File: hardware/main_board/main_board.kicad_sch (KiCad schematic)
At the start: 4 parts

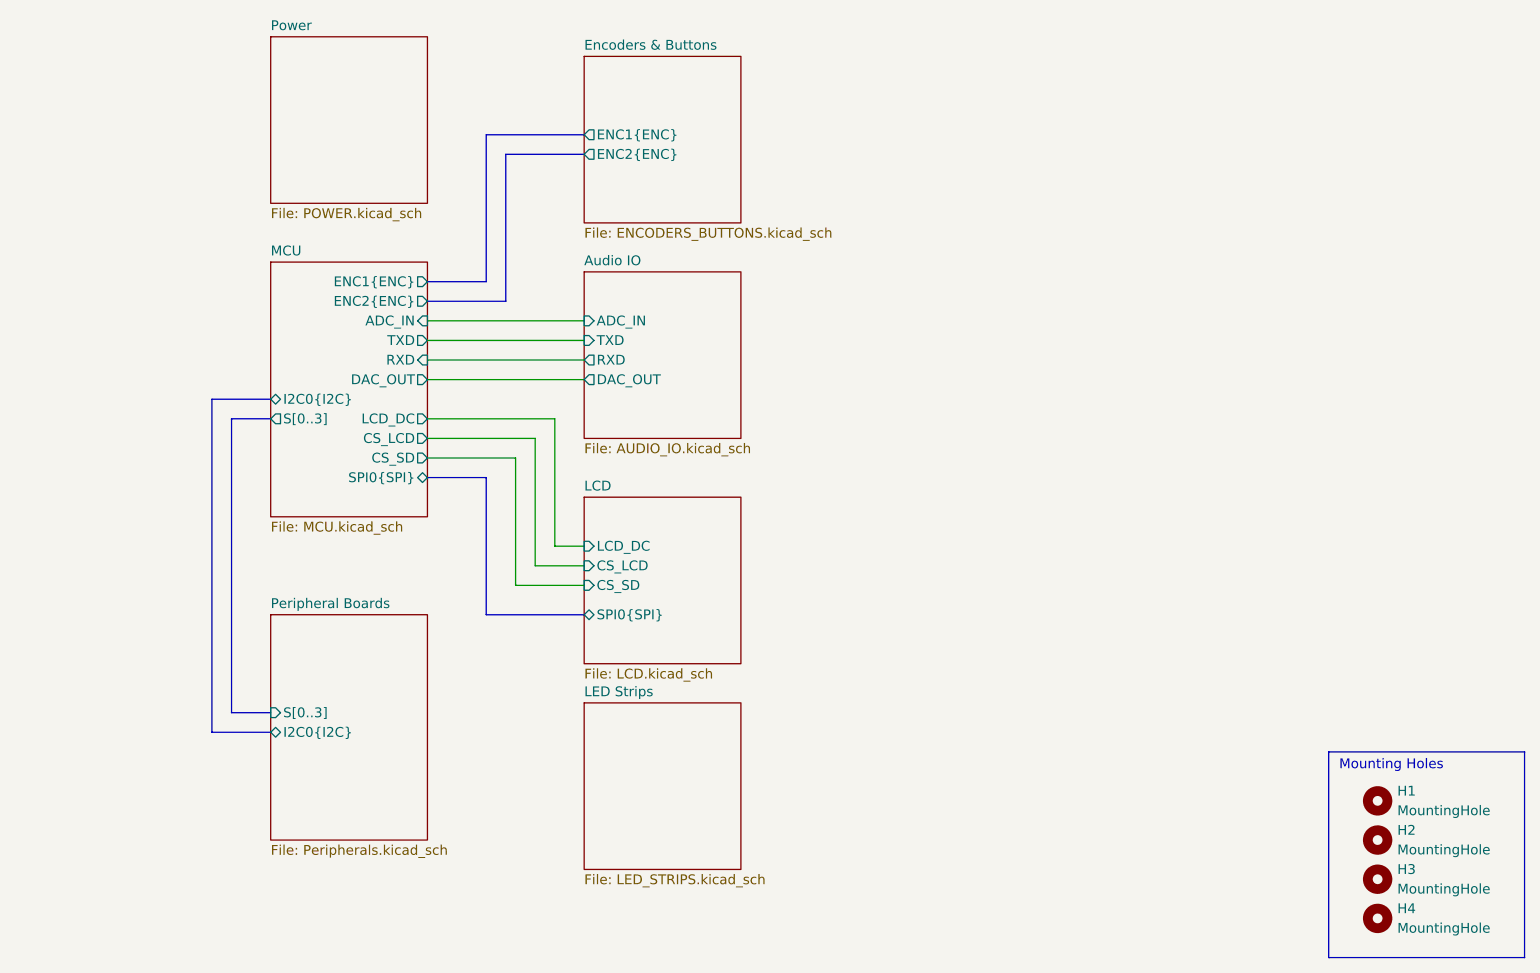
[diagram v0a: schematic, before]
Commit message: added lakshay suggestions to peripheral board. removed bypass jumper from main board audio amp. added led strip interface. added too many things to remember i forgor
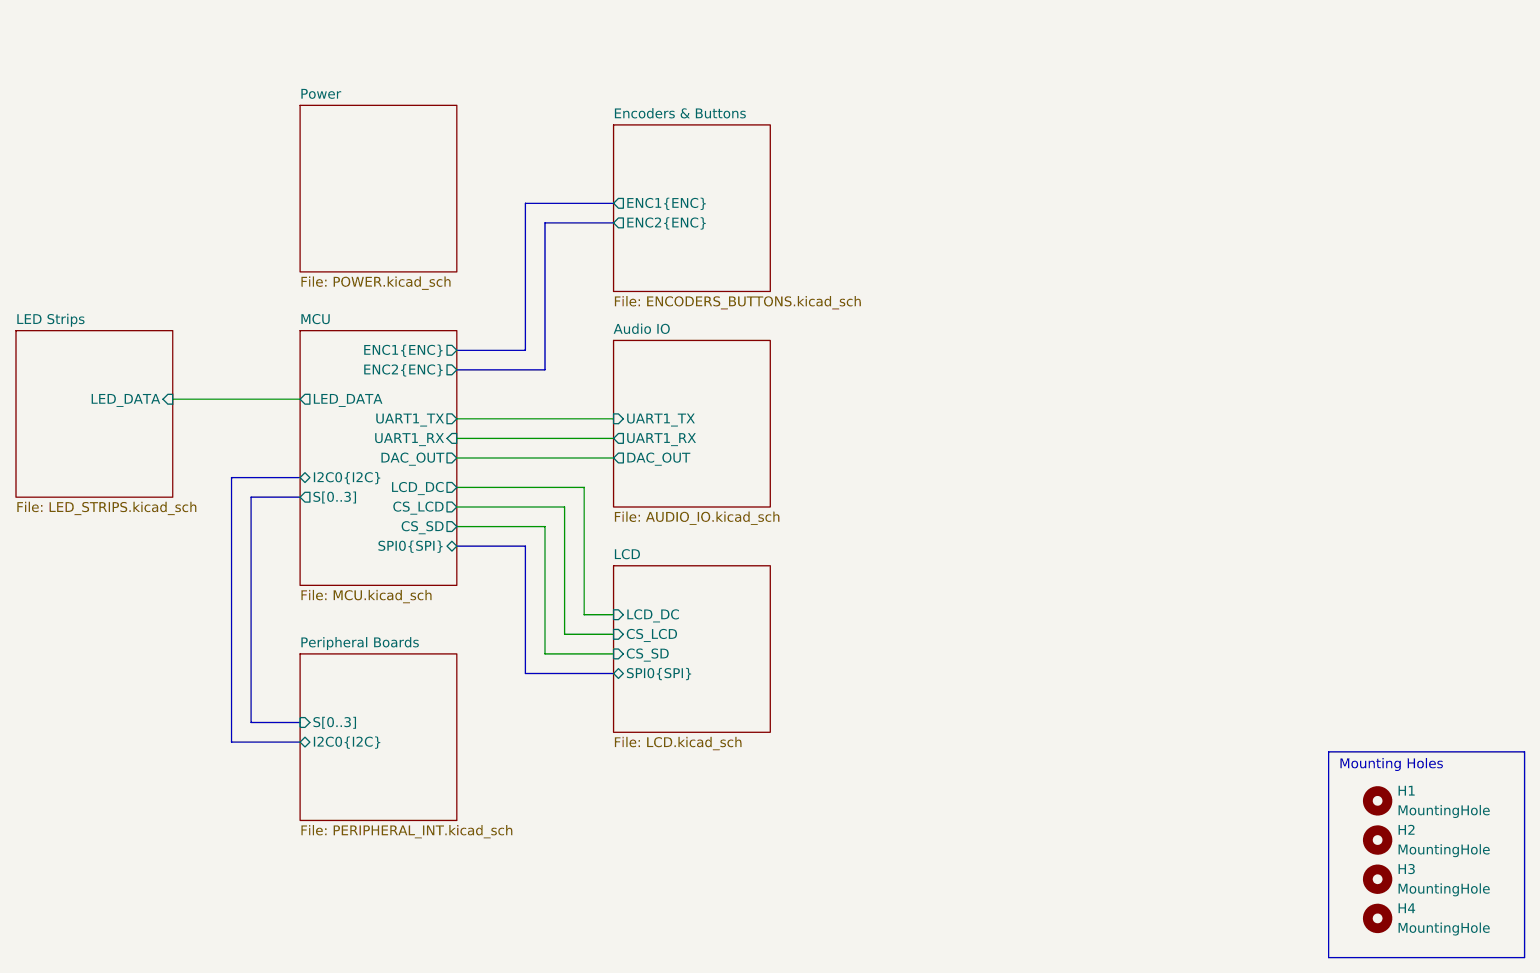
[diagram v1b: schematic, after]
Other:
- sheet Audio IO ports: added UART1_RX, UART1_TX; removed ADC_IN, RXD, TXD
- sheet LED Strips ports: added LED_DATA; removed none
- sheet MCU ports: added LED_DATA, UART1_RX, UART1_TX; removed ADC_IN, RXD, TXD
- sheet Peripheral Boards: file Peripherals.kicad_sch -> PERIPHERAL_INT.kicad_sch
